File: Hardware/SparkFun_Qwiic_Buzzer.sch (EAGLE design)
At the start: 48 parts, among them J2 QWIIC_RA, J3 QWIIC_RA, Q3 200mA/40V, U4 ATTINY84-ARDUINO

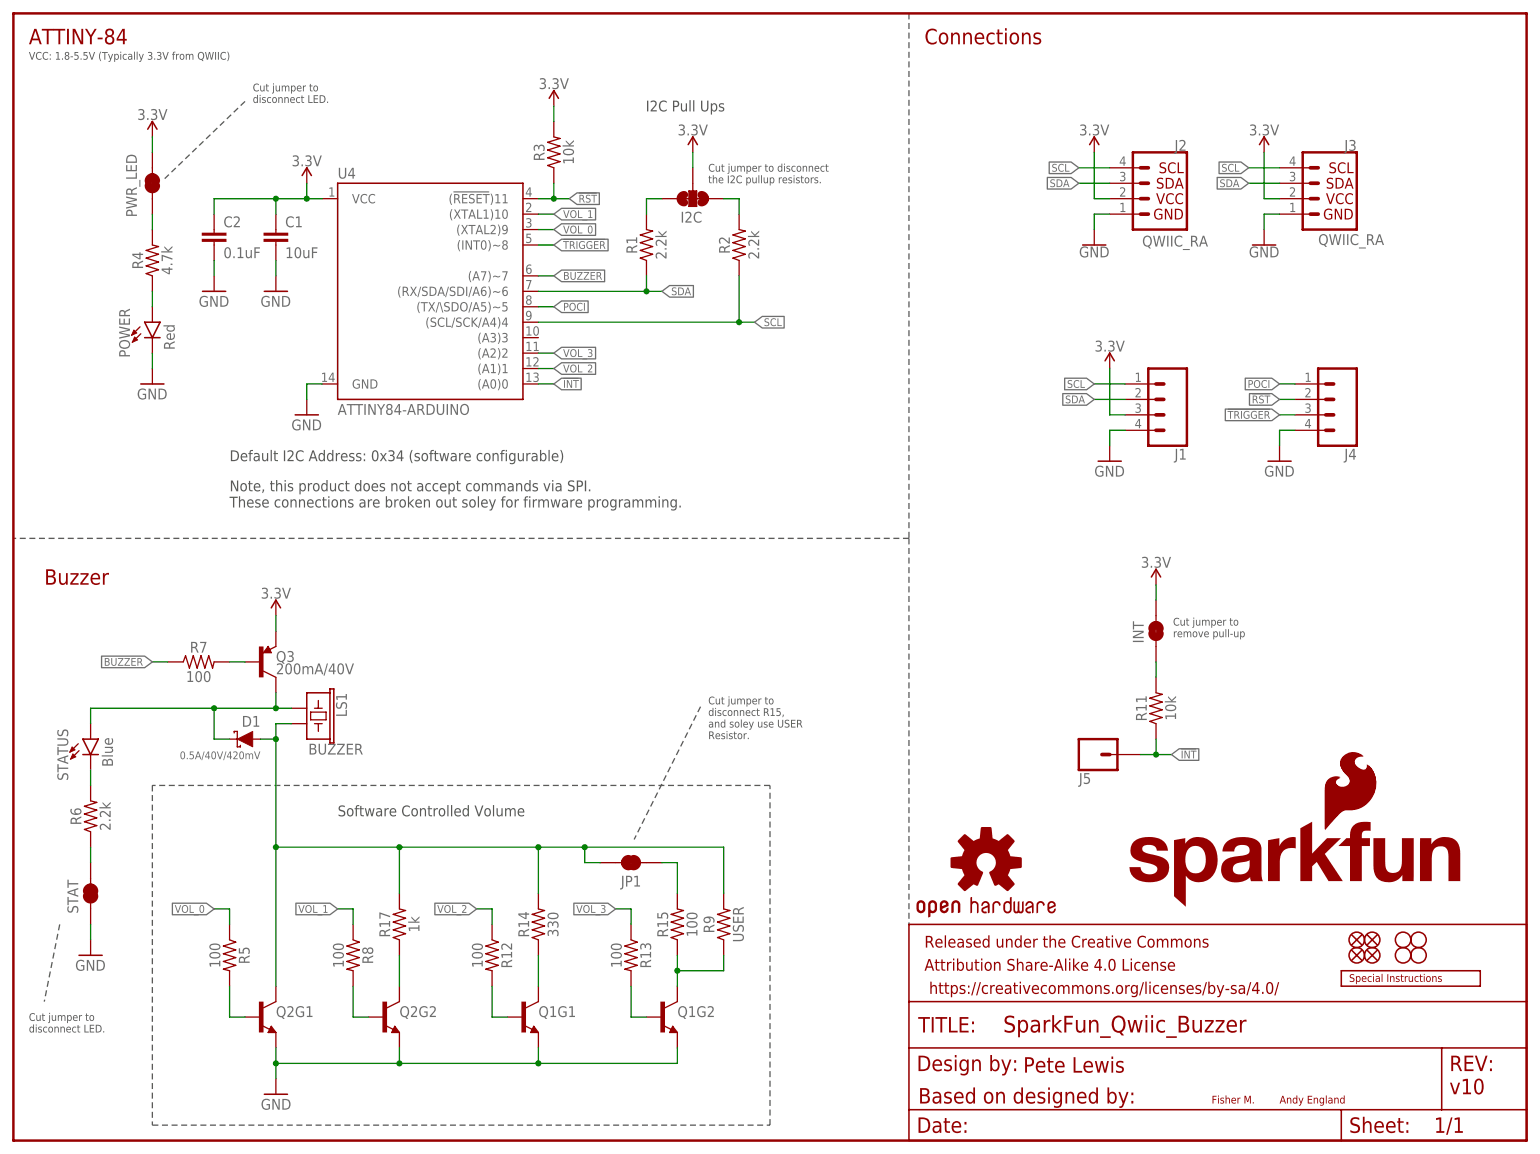
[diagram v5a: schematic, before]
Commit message: post review tweaks
-removed INT pin feature (both header pin and pullup resistor)
-changed TRIGGER pin to use POCI pin. It will be there for programming as needed, but this naming omits any mention of SPI, making it really clear this doesn't do SPI.
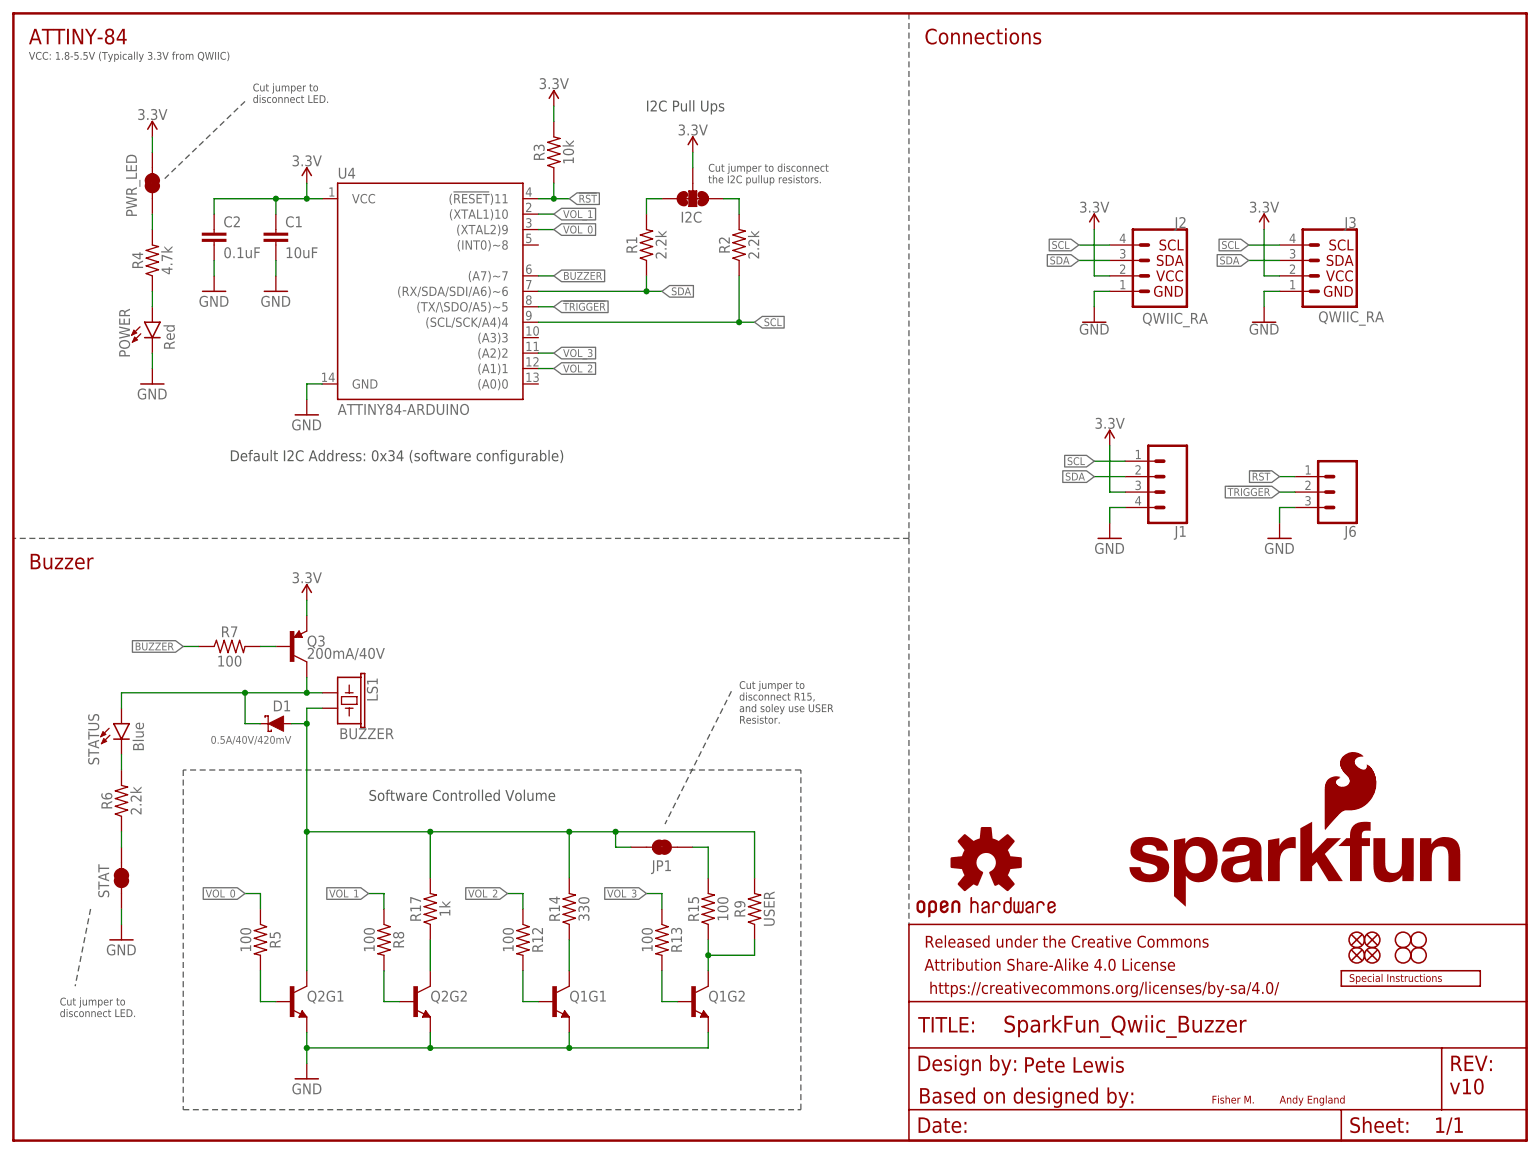
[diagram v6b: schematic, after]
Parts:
- removed INT: JUMPER-SMT_2_NC_TRACE_SILK, SparkFun-Jumpers:JUMPER-SMT_2_NC_TRACE_SILK
- removed J4: (no value), SparkFun-Connectors:CONN_041X04_NO_SILK
- removed J5: (no value), SparkFun-Connectors:CONN_01PTH_NO_SILK_YES_STOP
- removed R11: 10k, SparkFun-Resistors:10KOHM-0402T-1/16W-1%
- added J6: (no value), SparkFun-Connectors:CONN_031X03_NO_SILK
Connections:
- removed net !INT: J5.1, R11.1, U4.(A0)0
- removed net INT_R: INT.1, R11.2
- removed net POCI: J4.1, U4.(TX/\SDO/A5)~5
- net !RST: now also J6.1; no longer J4.2
- net !TRIGGER!: now also J6.2, U4.(TX/\SDO/A5)~5; no longer J4.3, U4.(INT0)~8
- net 3.3V: no longer INT.2
- net GND: now also J6.3; no longer J4.4
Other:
- note removed: "Cut jumper to remove pull-up"
- note removed: "Note, this product does not accept commands via SPI. These connections are broken out soley for firmware programming."
- moved on the sheet: D1, J1, J2, J3, JP1, LS1, Q1G1, Q1G2, Q2G1, Q2G2, Q3, R12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

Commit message: finalized resistor values on vol control
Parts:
- R12, R13, R5, R7, R8: value 100 -> 330; device SparkFun-Resistors:100OHM-0402-TIGHT-1/16W-1% -> SparkFun-Resistors:330OHM-0402T-1/16W-5%
- R14: device SparkFun-Resistors:330OHM-0603-1/10W-1% -> SparkFun-Resistors:330OHM-0402T-1/16W-5%
- R15: device SparkFun-Resistors:100OHM-0603-1/10W-1% -> SparkFun-Resistors:100OHM-0402-TIGHT-1/16W-1%
- R17: value 1k -> 2.2k; device SparkFun-Resistors:1KOHM-0603-1/10W-1% -> SparkFun-Resistors:2.2KOHM-0402T-1/16W-1%
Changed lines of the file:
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@@
 <part name="LOGO4" library="SparkFun-Aesthetics" deviceset="SFE_LOGO_FLAME" device=".1_INCH"/>
 <part name="LS1" library="SparkFun-Electromechanical" deviceset="BUZZER" device="-SMD" value="BUZZER"/>
-<part name="R5" library="SparkFun-Resistors" deviceset="100OHM" device="-0402-TIGHT-1/16W-1%" value="100"/>
+<part name="R5" library="SparkFun-Resistors" deviceset="330OHM" device="-0402T-1/16W-5%" value="330"/>
 <part name="PWR_LED" library="SparkFun-Jumpers" deviceset="JUMPER-SMT_2_NC_TRACE" device="_SILK" package3d_urn="urn:adsk.eagle:package:39281/1" value="PWR_LED"/>
 <part name="SUPPLY3" library="SparkFun-PowerSymbols" deviceset="3.3V" device=""/>
@@
 <part name="Q2" library="SparkFun-DiscreteSemi" deviceset="TRANS_NPN_DUAL" device="-MBT3904DW1T1"/>
 <part name="Q3" library="SparkFun-DiscreteSemi" deviceset="TRANS_PNP" device="-PMBT3906|MMBT3906L" value="200mA/40V"/>
-<part name="R7" library="SparkFun-Resistors" deviceset="100OHM" device="-0402-TIGHT-1/16W-1%" value="100"/>
+<part name="R7" library="SparkFun-Resistors" deviceset="330OHM" device="-0402T-1/16W-5%" value="330"/>
 <part name="Q1" library="SparkFun-DiscreteSemi" deviceset="TRANS_NPN_DUAL" device="-MBT3904DW1T1"/>
 <part name="SUPPLY4" library="SparkFun-PowerSymbols" deviceset="3.3V" device=""/>
-<part name="R8" library="SparkFun-Resistors" deviceset="100OHM" device="-0402-TIGHT-1/16W-1%" value="100"/>
-<part name="R12" library="SparkFun-Resistors" deviceset="100OHM" device="-0402-TIGHT-1/16W-1%" value="100"/>
-<part name="R13" library="SparkFun-Resistors" deviceset="100OHM" device="-0402-TIGHT-1/16W-1%" value="100"/>
-<part name="R17" library="SparkFun-Resistors" deviceset="1KOHM" device="-0603-1/10W-1%" value="1k"/>
-<part name="R14" library="SparkFun-Resistors" deviceset="330OHM" device="-0603-1/10W-1%" value="330"/>
-<part name="R15" library="SparkFun-Resistors" deviceset="100OHM" device="-0603-1/10W-1%" value="100"/>
+<part name="R8" library="SparkFun-Resistors" deviceset="330OHM" device="-0402T-1/16W-5%" value="330"/>
+<part name="R12" library="SparkFun-Resistors" deviceset="330OHM" device="-0402T-1/16W-5%" value="330"/>
+<part name="R13" library="SparkFun-Resistors" deviceset="330OHM" device="-0402T-1/16W-5%" value="330"/>
+<part name="R17" library="SparkFun-Resistors" deviceset="2.2KOHM" device="-0402T-1/16W-1%" value="2.2k"/>
+<part name="R14" library="SparkFun-Resistors" deviceset="330OHM" device="-0402T-1/16W-5%" value="330"/>
+<part name="R15" library="SparkFun-Resistors" deviceset="100OHM" device="-0402-TIGHT-1/16W-1%" value="100"/>
 <part name="GND1" library="SparkFun-PowerSymbols" deviceset="GND" device=""/>
 <part name="H3" library="SparkFun-Hardware" deviceset="STAND-OFF" device=""/>

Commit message: STAT LED moved to GPIO
-This way it won't be dimmed by the buzzers frequency and can more precisely be controlled via firmware.
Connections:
- new net STAT: STATUS.A, U4.(A0)0
- net N$6: no longer STATUS.A
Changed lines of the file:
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@@
 <part name="GND8" library="SparkFun-PowerSymbols" deviceset="GND" device=""/>
 <part name="SUPPLY12" library="SparkFun-PowerSymbols" deviceset="3.3V" device=""/>
-<part name="J1" library="SparkFun-Connectors" deviceset="CONN_04" device="1X04_NO_SILK"/>
+<part name="J1" library="SparkFun-Connectors" deviceset="CONN_04" device="1X04_NO_SILK">
+<attribute name="PROD_ID" value=""/>
+</part>
 <part name="GND7" library="SparkFun-PowerSymbols" deviceset="GND" device=""/>
 <part name="C2" library="SparkFun-Capacitors" deviceset="0.1UF" device="-0402T-16V-10%" value="0.1uF"/>
@@
 <pinref part="Q3" gate="G$1" pin="C"/>
 <wire x1="48.26" y1="73.66" x2="48.26" y2="76.2" width="0.1524" layer="91"/>
-<pinref part="STATUS" gate="G$1" pin="A"/>
 <wire x1="48.26" y1="73.66" x2="38.1" y2="73.66" width="0.1524" layer="91"/>
-<wire x1="38.1" y1="73.66" x2="17.78" y2="73.66" width="0.1524" layer="91"/>
-<wire x1="17.78" y1="73.66" x2="17.78" y2="71.12" width="0.1524" layer="91"/>
 <junction x="48.26" y="73.66"/>
 <pinref part="D1" gate="G$1" pin="C"/>
 <wire x1="40.64" y1="68.58" x2="38.1" y2="68.58" width="0.1524" layer="91"/>
 <wire x1="38.1" y1="68.58" x2="38.1" y2="73.66" width="0.1524" layer="91"/>
-<junction x="38.1" y="73.66"/>
 </segment>
 </net>
@@
 </segment>
 </net>
+<net name="STAT" class="0">
+<segment>
+<pinref part="STATUS" gate="G$1" pin="A"/>
+<wire x1="17.78" y1="71.12" x2="17.78" y2="73.66" width="0.1524" layer="91"/>
+<wire x1="17.78" y1="73.66" x2="15.24" y2="73.66" width="0.1524" layer="91"/>
+<label x="15.24" y="73.66" size="1.27" layer="95" font="vector" rot="R180" xref="yes"/>
+</segment>
+<segment>
+<pinref part="U4" gate="U1" pin="(A0)0"/>
+<wire x1="86.36" y1="124.46" x2="88.9" y2="124.46" width="0.1524" layer="91"/>
+<label x="88.9" y="124.46" size="1.27" layer="95" font="vector" xref="yes"/>
+</segment>
+</net>
